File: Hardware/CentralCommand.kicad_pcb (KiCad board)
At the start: 4 copper layers, 54 parts, among them IC101 STM32F030C8, IC201 FT232RQ, P101 I2C, P102 GPIO1, P103 GPIO1, P104 USART, P105 SPI, P106 ADC, P201 USB_OTG, P202 POWER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

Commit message: converted VCCIO to 3V3 and added 1x2 power and gnd
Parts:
- added P203: 3V3, Pin_Headers:Pin_Header_Straight_1x02, F.Cu at (126.2, 56.9)
- C107: footprint Capacitors_SMD:C_1206 -> Capacitors_SMD:C_0805
- R205, R206: value 330 -> 270
- R306, R307: value 10K -> 4.7K
- TP201: value TEST -> V-IN
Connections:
- IC201 pad 1: Net-(C202-Pad1) -> Net-(C204-Pad1)
- R205 pad 2: Net-(C202-Pad1) -> Net-(C204-Pad1)
- R206 pad 2: Net-(C202-Pad1) -> Net-(C204-Pad1)
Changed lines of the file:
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@@
 (kicad_pcb (version 4) (host pcbnew 4.0.5)
   (general
-    (links 154)
-    (no_connects 121)
-    (area 97.8916 61.1886 155.727401 131.597401)
+    (links 156)
+    (no_connects 124)
+    (area 0 0 0 0)
     (thickness 1.6)
     (drawings 0)
     (tracks 76)
     (zones 0)
-    (modules 54)
+    (modules 55)
     (nets 66)
   )
@@
     )
   )
-  (module Capacitors_SMD:C_1206 (layer F.Cu)
-    (at 123.2027 100.6094 180)
-    (descr "Capacitor SMD 1206, reflow soldering, AVX (see smccp.pdf)")
-    (tags "capacitor 1206")
-    (attr smd)
-    (fp_text reference C107 (at 0 -2.3 180) (layer F.SilkS)
-      (effects (font (size 1 1) (thickness 0.15)))
-    )
-    (fp_text value 10nF (at 0 2.3 180) (layer F.Fab)
-      (effects (font (size 1 1) (thickness 0.15)))
-    )
-    (fp_line (start -1.6 0.8) (end -1.6 -0.8) (layer F.Fab) (width 0.15))
-    (fp_line (start 1.6 0.8) (end -1.6 0.8) (layer F.Fab) (width 0.15))
-    (fp_line (start 1.6 -0.8) (end 1.6 0.8) (layer F.Fab) (width 0.15))
-    (fp_line (start -1.6 -0.8) (end 1.6 -0.8) (layer F.Fab) (width 0.15))
-    (fp_line (start -2.3 -1.15) (end 2.3 -1.15) (layer F.CrtYd) (width 0.05))
-    (fp_line (start -2.3 1.15) (end 2.3 1.15) (layer F.CrtYd) (width 0.05))
-    (fp_line (start -2.3 -1.15) (end -2.3 1.15) (layer F.CrtYd) (width 0.05))
-    (fp_line (start 2.3 -1.15) (end 2.3 1.15) (layer F.CrtYd) (width 0.05))
-    (fp_line (start 1 -1.025) (end -1 -1.025) (layer F.SilkS) (width 0.15))
-    (fp_line (start -1 1.025) (end 1 1.025) (layer F.SilkS) (width 0.15))
-    (pad 1 smd rect (at -1.5 0 180) (size 1 1.6) (layers F.Cu F.Paste F.Mask)
-      (net 5 "Net-(C107-Pad1)"))
-    (pad 2 smd rect (at 1.5 0 180) (size 1 1.6) (layers F.Cu F.Paste F.Mask)
-      (net 2 GND))
-    (model Capacitors_SMD.3dshapes/C_1206.wrl
-      (at (xyz 0 0 0))
-      (scale (xyz 1 1 1))
-      (rotate (xyz 0 0 0))
-    )
-  )
   (module Capacitors_SMD:C_0805 (layer F.Cu)
     (at 126.9873 101.7905 90)
@@
     (fp_line (start 2.625 -2.625) (end 2.1 -2.625) (layer F.SilkS) (width 0.15))
     (pad 1 smd rect (at -2.4 -1.75 180) (size 0.7 0.25) (layers F.Cu F.Paste F.Mask)
-      (net 7 "Net-(C202-Pad1)"))
+      (net 8 "Net-(C204-Pad1)"))
     (pad 2 smd rect (at -2.4 -1.25 180) (size 0.7 0.25) (layers F.Cu F.Paste F.Mask)
       (net 35 "Net-(IC201-Pad2)"))
@@
       (effects (font (size 1 1) (thickness 0.15)) (justify mirror))
     )
-    (fp_text value 330 (at 0 -2.1 270) (layer B.Fab)
+    (fp_text value 270 (at 0 -2.1 270) (layer B.Fab)
       (effects (font (size 1 1) (thickness 0.15)) (justify mirror))
     )
@@
       (net 12 "Net-(D203-Pad2)"))
     (pad 2 smd rect (at 0.95 0 270) (size 0.7 1.3) (layers B.Cu B.Paste B.Mask)
-      (net 7 "Net-(C202-Pad1)"))
+      (net 8 "Net-(C204-Pad1)"))
     (model Resistors_SMD.3dshapes/R_0805.wrl
       (at (xyz 0 0 0))
@@
       (effects (font (size 1 1) (thickness 0.15)) (justify mirror))
     )
-    (fp_text value 330 (at 0 -2.1 270) (layer B.Fab)
+    (fp_text value 270 (at 0 -2.1 270) (layer B.Fab)
       (effects (font (size 1 1) (thickness 0.15)) (justify mirror))
     )
@@
       (net 14 "Net-(D204-Pad2)"))
     (pad 2 smd rect (at 0.95 0 270) (size 0.7 1.3) (layers B.Cu B.Paste B.Mask)
-      (net 7 "Net-(C202-Pad1)"))
+      (net 8 "Net-(C204-Pad1)"))
     (model Resistors_SMD.3dshapes/R_0805.wrl
       (at (xyz 0 0 0))
@@
       (effects (font (size 1 1) (thickness 0.15)))
     )
-    (fp_text value 10K (at 0 2.1) (layer F.Fab)
+    (fp_text value 4.7K (at 0 2.1) (layer F.Fab)
       (effects (font (size 1 1) (thickness 0.15)))
     )
@@
       (effects (font (size 1 1) (thickness 0.15)))
     )
-    (fp_text value 10K (at 0 2.1) (layer F.Fab)
+    (fp_text value 4.7K (at 0 2.1) (layer F.Fab)
       (effects (font (size 1 1) (thickness 0.15)))
     )
@@
       (effects (font (size 1 1) (thickness 0.15)))
     )
-    (fp_text value TEST (at 0 2) (layer F.Fab)
+    (fp_text value V-IN (at 0 2) (layer F.Fab)
       (effects (font (size 1 1) (thickness 0.15)))
     )
@@
       (net 3 "Net-(C102-Pad1)"))
   )
-  (segment (start 128.7018 67.9417) (end 126.9078 67.9417) (width 0.127) (layer B.Cu) (net 2) (status 400000))
+  (module Capacitors_SMD:C_0805 (layer F.Cu)
+    (at 123.2027 100.6094 180)
+    (descr "Capacitor SMD 0805, reflow soldering, AVX (see smccp.pdf)")
+    (tags "capacitor 0805")
+    (attr smd)
+    (fp_text reference C107 (at 0 -2.1 180) (layer F.SilkS)
+      (effects (font (size 1 1) (thickness 0.15)))
+    )
+    (fp_text value 10nF (at 0 2.1 180) (layer F.Fab)
+      (effects (font (size 1 1) (thickness 0.15)))
+    )
+    (fp_line (start -1 0.625) (end -1 -0.625) (layer F.Fab) (width 0.15))
+    (fp_line (start 1 0.625) (end -1 0.625) (layer F.Fab) (width 0.15))
+    (fp_line (start 1 -0.625) (end 1 0.625) (layer F.Fab) (width 0.15))
+    (fp_line (start -1 -0.625) (end 1 -0.625) (layer F.Fab) (width 0.15))
+    (fp_line (start -1.8 -1) (end 1.8 -1) (layer F.CrtYd) (width 0.05))
+    (fp_line (start -1.8 1) (end 1.8 1) (layer F.CrtYd) (width 0.05))
+    (fp_line (start -1.8 -1) (end -1.8 1) (layer F.CrtYd) (width 0.05))
+    (fp_line (start 1.8 -1) (end 1.8 1) (layer F.CrtYd) (width 0.05))
+    (fp_line (start 0.5 -0.85) (end -0.5 -0.85) (layer F.SilkS) (width 0.15))
+    (fp_line (start -0.5 0.85) (end 0.5 0.85) (layer F.SilkS) (width 0.15))
+    (pad 1 smd rect (at -1 0 180) (size 1 1.25) (layers F.Cu F.Paste F.Mask)
+      (net 5 "Net-(C107-Pad1)"))
+    (pad 2 smd rect (at 1 0 180) (size 1 1.25) (layers F.Cu F.Paste F.Mask)
+      (net 2 GND))
+    (model Capacitors_SMD.3dshapes/C_0805.wrl
+      (at (xyz 0 0 0))
+      (scale (xyz 1 1 1))
+      (rotate (xyz 0 0 0))
+    )
+  )
+  (module Pin_Headers:Pin_Header_Straight_1x02 (layer F.Cu)
+    (at 126.238 56.896)
+    (descr "Through hole pin header")
+    (tags "pin header")
+    (fp_text reference P203 (at 0 -5.1) (layer F.SilkS)
+      (effects (font (size 1 1) (thickness 0.15)))
+    )
+    (fp_text value 3V3 (at 0 -3.1) (layer F.Fab)
+      (effects (font (size 1 1) (thickness 0.15)))
+    )
+    (fp_line (start 1.27 1.27) (end 1.27 3.81) (layer F.SilkS) (width 0.15))
+    (fp_line (start 1.55 -1.55) (end 1.55 0) (layer F.SilkS) (width 0.15))
+    (fp_line (start -1.75 -1.75) (end -1.75 4.3) (layer F.CrtYd) (width 0.05))
+    (fp_line (start 1.75 -1.75) (end 1.75 4.3) (layer F.CrtYd) (width 0.05))
+    (fp_line (start -1.75 -1.75) (end 1.75 -1.75) (layer F.CrtYd) (width 0.05))
+    (fp_line (start -1.75 4.3) (end 1.75 4.3) (layer F.CrtYd) (width 0.05))
+    (fp_line (start 1.27 1.27) (end -1.27 1.27) (layer F.SilkS) (width 0.15))
+    (fp_line (start -1.55 0) (end -1.55 -1.55) (layer F.SilkS) (width 0.15))
+    (fp_line (start -1.55 -1.55) (end 1.55 -1.55) (layer F.SilkS) (width 0.15))
+    (fp_line (start -1.27 1.27) (end -1.27 3.81) (layer F.SilkS) (width 0.15))
+    (fp_line (start -1.27 3.81) (end 1.27 3.81) (layer F.SilkS) (width 0.15))
+    (pad 1 thru_hole rect (at 0 0) (size 2.032 2.032) (drill 1.016) (layers *.Cu *.Mask)
+      (net 4 /PWR))
+    (pad 2 thru_hole oval (at 0 2.54) (size 2.032 2.032) (drill 1.016) (layers *.Cu *.Mask)
+      (net 2 GND))
+    (model Pin_Headers.3dshapes/Pin_Header_Straight_1x02.wrl
+      (at (xyz 0 -0.05 0))
+      (scale (xyz 1 1 1))
+      (rotate (xyz 0 0 90))
+    )
+  )
+  (segment (start 128.7018 67.9417) (end 126.9078 67.9417) (width 0.127) (layer B.Cu) (net 2))
   (via (at 126.8857 67.9196) (size 0.4572) (drill 0.254) (layers F.Cu B.Cu) (net 2))
   (segment (start 126.9078 67.9417) (end 126.8857 67.9196) (width 0.127) (layer B.Cu) (net 2))
-  (segment (start 132.817 67.7915) (end 131.9033 67.7915) (width 0.127) (layer F.Cu) (net 2) (status 400000))
+  (segment (start 132.817 67.7915) (end 131.9033 67.7915) (width 0.127) (layer F.Cu) (net 2))
   (via (at 131.2672 68.4276) (size 0.4572) (drill 0.254) (layers F.Cu B.Cu) (net 2))
   (segment (start 131.9033 67.7915) (end 131.2672 68.4276) (width 0.127) (layer F.Cu) (net 2))
-  (segment (start 139.217 67.7915) (end 140.499 67.7915) (width 0.127) (layer F.Cu) (net 2) (status 400000))
+  (segment (start 139.217 67.7915) (end 140.499 67.7915) (width 0.127) (layer F.Cu) (net 2))
   (via (at 140.5509 67.8434) (size 0.4572) (drill 0.254) (layers F.Cu B.Cu) (net 2))
   (segment (start 140.499 67.7915) (end 140.5509 67.8434) (width 0.127) (layer F.Cu) (net 2))
-  (segment (start 132.4966 70.8914) (end 132.6769 70.8914) (width 0.127) (layer F.Cu) (net 2) (status C00000))
-  (segment (start 132.6769 70.8914) (end 133.4516 70.1167) (width 0.127) (layer F.Cu) (net 2) (status 400000))
+  (segment (start 132.4966 70.8914) (end 132.6769 70.8914) (width 0.127) (layer F.Cu) (net 2))
+  (segment (start 132.6769 70.8914) (end 133.4516 70.1167) (width 0.127) (layer F.Cu) (net 2))
   (via (at 133.4516 70.1167) (size 0.4572) (drill 0.254) (layers F.Cu B.Cu) (net 2))
   (segment (start 137.217 65.3415) (end 137.217 65.7915) (width 0.127) (layer F.Cu) (net 2))
@@
   (segment (start 137.317 66.8447) (end 136.9822 66.5099) (width 0.127) (layer F.Cu) (net 6))
   (segment (start 128.0828 65.9417) (end 128.7018 65.9417) (width 0.127) (layer B.Cu) (net 6))
-  (segment (start 128.7396 75.1052) (end 129.1616 75.1052) (width 0.127) (layer F.Cu) (net 7))
   (segment (start 132.9477 72.2249) (end 134.7384 70.4342) (width 0.127) (layer F.Cu) (net 7))
   (segment (start 132.0419 72.2249) (end 132.9477 72.2249) (width 0.127) (layer F.Cu) (net 7))
   (segment (start 129.1616 75.1052) (end 132.0419 72.2249) (width 0.127) (layer F.Cu) (net 7))
+  (segment (start 128.7396 75.1052) (end 129.1616 75.1052) (width 0.127) (layer F.Cu) (net 8))
   (segment (start 137.9474 71.8693) (end 137.9474 72.898) (width 0.127) (layer F.Cu) (net 9))
   (segment (start 138.3665 73.3171) (end 139.2588 73.3171) (width 0.127) (layer F.Cu) (net 9))

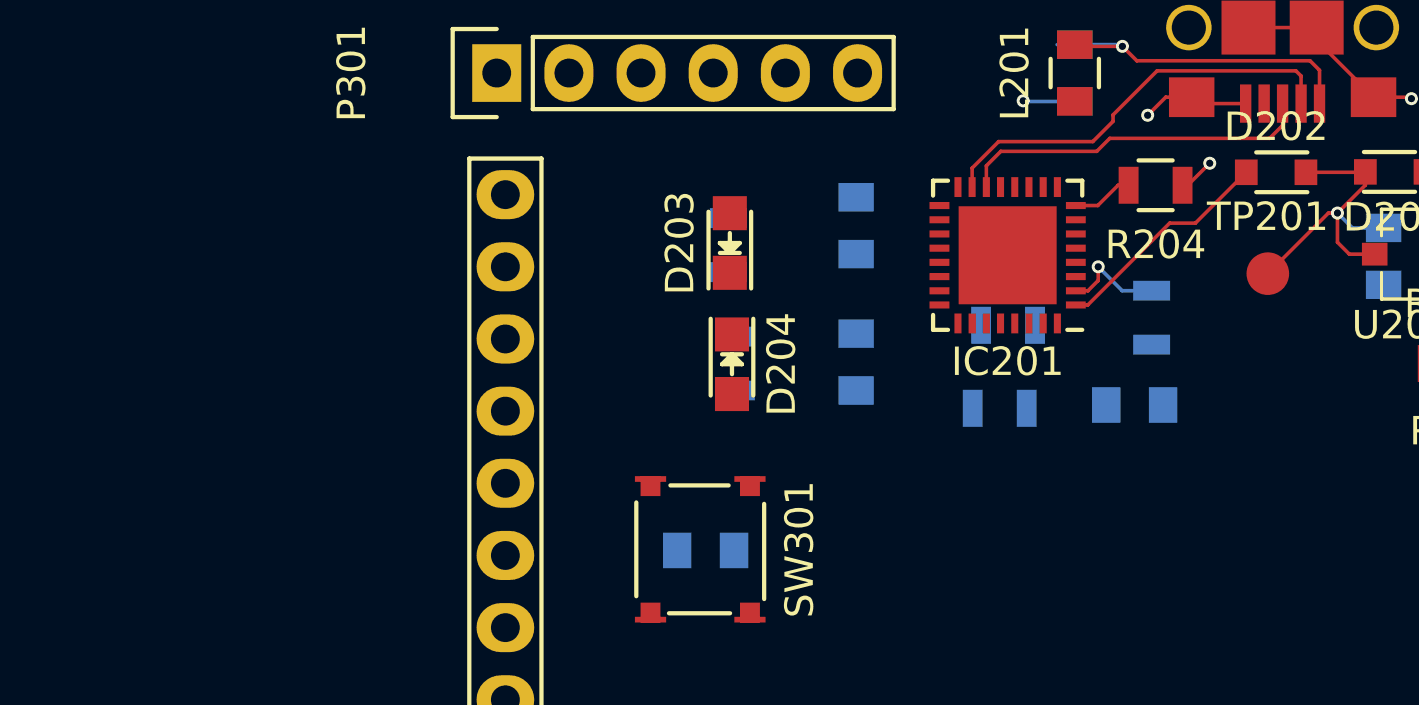
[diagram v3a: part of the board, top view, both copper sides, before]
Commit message: swapped power and gnd on gpio headers and added blinky led
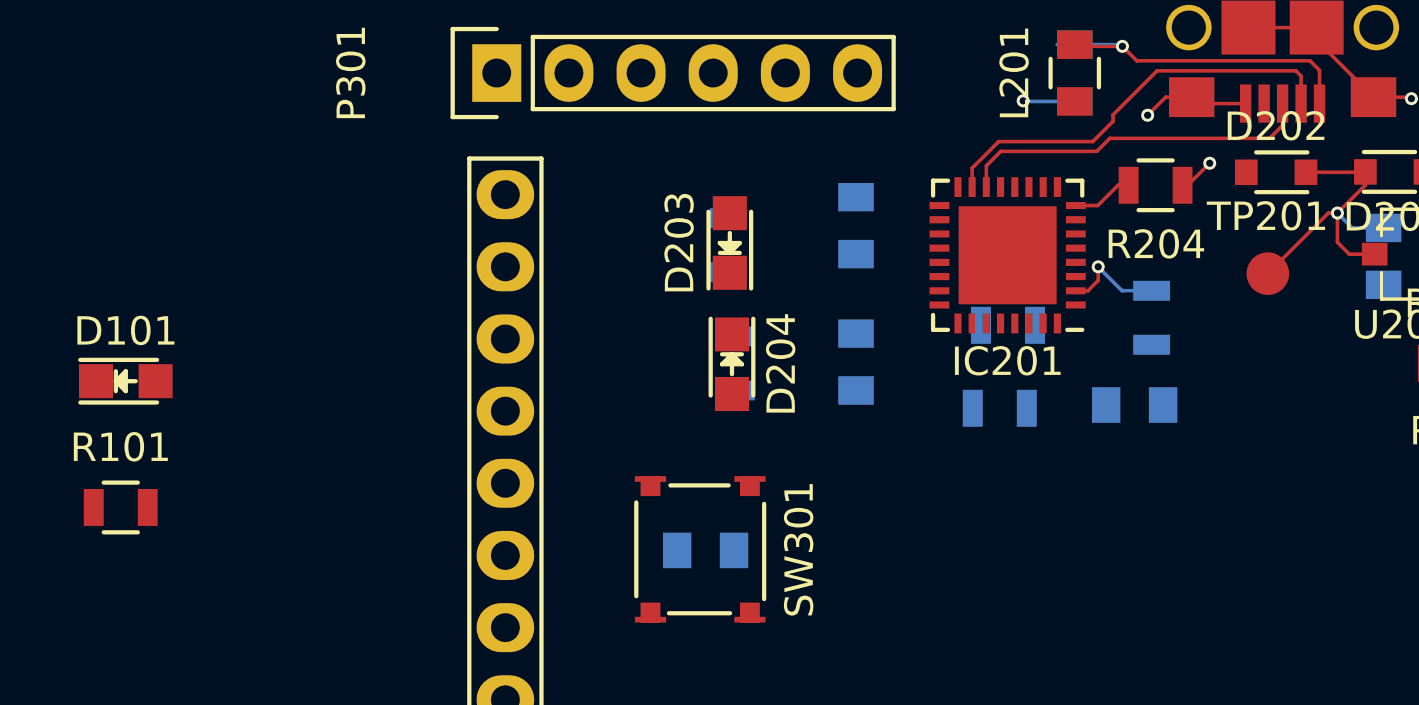
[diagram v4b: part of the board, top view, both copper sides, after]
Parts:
- added D101: RED LED, LEDs:LED_0805, F.Cu at (95.3, 77.8)
- added R101: 270, Resistors_SMD:R_0805, F.Cu at (95.1, 82.2)
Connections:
- P102 pad 1: GND -> /PWR
- P102 pad 2: /PWR -> GND
- P103 pad 1: GND -> /PWR
- P103 pad 2: /PWR -> GND
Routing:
- net Net-(C202-Pad1): track 7.51 -> 0.00 mm
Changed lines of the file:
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@@
 (kicad_pcb (version 4) (host pcbnew 4.0.5)
   (general
-    (links 156)
-    (no_connects 124)
+    (links 159)
+    (no_connects 129)
     (area 0 0 0 0)
     (thickness 1.6)
     (drawings 0)
-    (tracks 76)
+    (tracks 72)
     (zones 0)
-    (modules 55)
-    (nets 66)
+    (modules 57)
+    (nets 67)
   )
   (page A4)
@@
   (net 64 "Net-(IC201-Pad14)")
   (net 65 "Net-(IC201-Pad15)")
+  (net 66 "Net-(D101-Pad2)")
   (net_class Default "This is the default net class."
     (clearance 0.127)
@@
     (add_net "Net-(C204-Pad1)")
     (add_net "Net-(C205-Pad1)")
+    (add_net "Net-(D101-Pad2)")
     (add_net "Net-(D201-Pad2)")
     (add_net "Net-(D203-Pad2)")
@@
     (fp_line (start -1.55 -1.55) (end 1.55 -1.55) (layer F.SilkS) (width 0.15))
     (pad 1 thru_hole rect (at 0 0 180) (size 2.032 1.7272) (drill 1.016) (layers *.Cu *.Mask)
-      (net 2 GND))
+      (net 4 /PWR))
     (pad 2 thru_hole oval (at 0 2.54 180) (size 2.032 1.7272) (drill 1.016) (layers *.Cu *.Mask)
-      (net 4 /PWR))
+      (net 2 GND))
     (pad 3 thru_hole oval (at 0 5.08 180) (size 2.032 1.7272) (drill 1.016) (layers *.Cu *.Mask)
       (net 44 /PC13))
@@
     (fp_line (start -1.55 -1.55) (end 1.55 -1.55) (layer F.SilkS) (width 0.15))
     (pad 1 thru_hole rect (at 0 0 180) (size 2.032 1.7272) (drill 1.016) (layers *.Cu *.Mask)
-      (net 2 GND))
+      (net 4 /PWR))
     (pad 2 thru_hole oval (at 0 2.54 180) (size 2.032 1.7272) (drill 1.016) (layers *.Cu *.Mask)
-      (net 4 /PWR))
+      (net 2 GND))
     (pad 3 thru_hole oval (at 0 5.08 180) (size 2.032 1.7272) (drill 1.016) (layers *.Cu *.Mask)
       (net 60 /PA12))
@@
     )
   )
+  (module LEDs:LED_0805 (layer F.Cu)
+    (at 95.3008 77.7875)
+    (descr "LED 0805 smd package")
+    (tags "LED 0805 SMD")
+    (attr smd)
+    (fp_text reference D101 (at 0 -1.75) (layer F.SilkS)
+      (effects (font (size 1 1) (thickness 0.15)))
+    )
+    (fp_text value "RED LED" (at 0 1.75) (layer F.Fab)
+      (effects (font (size 1 1) (thickness 0.15)))
+    )
+    (fp_line (start -0.4 -0.3) (end -0.4 0.3) (layer F.Fab) (width 0.15))
+    (fp_line (start -0.3 0) (end 0 -0.3) (layer F.Fab) (width 0.15))
+    (fp_line (start 0 0.3) (end -0.3 0) (layer F.Fab) (width 0.15))
+    (fp_line (start 0 -0.3) (end 0 0.3) (layer F.Fab) (width 0.15))
+    (fp_line (start 1 -0.6) (end -1 -0.6) (layer F.Fab) (width 0.15))
+    (fp_line (start 1 0.6) (end 1 -0.6) (layer F.Fab) (width 0.15))
+    (fp_line (start -1 0.6) (end 1 0.6) (layer F.Fab) (width 0.15))
+    (fp_line (start -1 -0.6) (end -1 0.6) (layer F.Fab) (width 0.15))
+    (fp_line (start -1.6 0.75) (end 1.1 0.75) (layer F.SilkS) (width 0.15))
+    (fp_line (start -1.6 -0.75) (end 1.1 -0.75) (layer F.SilkS) (width 0.15))
+    (fp_line (start -0.1 0.15) (end -0.1 -0.1) (layer F.SilkS) (width 0.15))
+    (fp_line (start -0.1 -0.1) (end -0.25 0.05) (layer F.SilkS) (width 0.15))
+    (fp_line (start -0.35 -0.35) (end -0.35 0.35) (layer F.SilkS) (width 0.15))
+    (fp_line (start 0 0) (end 0.35 0) (layer F.SilkS) (width 0.15))
+    (fp_line (start -0.35 0) (end 0 -0.35) (layer F.SilkS) (width 0.15))
+    (fp_line (start 0 -0.35) (end 0 0.35) (layer F.SilkS) (width 0.15))
+    (fp_line (start 0 0.35) (end -0.35 0) (layer F.SilkS) (width 0.15))
+    (fp_line (start 1.9 -0.95) (end 1.9 0.95) (layer F.CrtYd) (width 0.05))
+    (fp_line (start 1.9 0.95) (end -1.9 0.95) (layer F.CrtYd) (width 0.05))
+    (fp_line (start -1.9 0.95) (end -1.9 -0.95) (layer F.CrtYd) (width 0.05))
+    (fp_line (start -1.9 -0.95) (end 1.9 -0.95) (layer F.CrtYd) (width 0.05))
+    (pad 2 smd rect (at 1.04902 0 180) (size 1.19888 1.19888) (layers F.Cu F.Paste F.Mask)
+      (net 66 "Net-(D101-Pad2)"))
+    (pad 1 smd rect (at -1.04902 0 180) (size 1.19888 1.19888) (layers F.Cu F.Paste F.Mask)
+      (net 2 GND))
+    (model LEDs.3dshapes/LED_0805.wrl
+      (at (xyz 0 0 0))
+      (scale (xyz 1 1 1))
+      (rotate (xyz 0 0 0))
+    )
+  )
+  (module Resistors_SMD:R_0805 (layer F.Cu)
+    (at 95.123 82.2325)
+    (descr "Resistor SMD 0805, reflow soldering, Vishay (see dcrcw.pdf)")
+    (tags "resistor 0805")
+    (attr smd)
+    (fp_text reference R101 (at 0 -2.1) (layer F.SilkS)
+      (effects (font (size 1 1) (thickness 0.15)))
+    )
+    (fp_text value 270 (at 0 2.1) (layer F.Fab)
+      (effects (font (size 1 1) (thickness 0.15)))
+    )
+    (fp_line (start -1 0.625) (end -1 -0.625) (layer F.Fab) (width 0.1))
+    (fp_line (start 1 0.625) (end -1 0.625) (layer F.Fab) (width 0.1))
+    (fp_line (start 1 -0.625) (end 1 0.625) (layer F.Fab) (width 0.1))
+    (fp_line (start -1 -0.625) (end 1 -0.625) (layer F.Fab) (width 0.1))
+    (fp_line (start -1.6 -1) (end 1.6 -1) (layer F.CrtYd) (width 0.05))
+    (fp_line (start -1.6 1) (end 1.6 1) (layer F.CrtYd) (width 0.05))
+    (fp_line (start -1.6 -1) (end -1.6 1) (layer F.CrtYd) (width 0.05))
+    (fp_line (start 1.6 -1) (end 1.6 1) (layer F.CrtYd) (width 0.05))
+    (fp_line (start 0.6 0.875) (end -0.6 0.875) (layer F.SilkS) (width 0.15))
+    (fp_line (start -0.6 -0.875) (end 0.6 -0.875) (layer F.SilkS) (width 0.15))
+    (pad 1 smd rect (at -0.95 0) (size 0.7 1.3) (layers F.Cu F.Paste F.Mask)
+      (net 58 /PB15))
+    (pad 2 smd rect (at 0.95 0) (size 0.7 1.3) (layers F.Cu F.Paste F.Mask)
+      (net 66 "Net-(D101-Pad2)"))
+    (model Resistors_SMD.3dshapes/R_0805.wrl
+      (at (xyz 0 0 0))
+      (scale (xyz 1 1 1))
+      (rotate (xyz 0 0 0))
+    )
+  )
   (segment (start 128.7018 67.9417) (end 126.9078 67.9417) (width 0.127) (layer B.Cu) (net 2))
   (via (at 126.8857 67.9196) (size 0.4572) (drill 0.254) (layers F.Cu B.Cu) (net 2))
@@
   (segment (start 137.317 66.8447) (end 136.9822 66.5099) (width 0.127) (layer F.Cu) (net 6))
   (segment (start 128.0828 65.9417) (end 128.7018 65.9417) (width 0.127) (layer B.Cu) (net 6))
-  (segment (start 132.9477 72.2249) (end 134.7384 70.4342) (width 0.127) (layer F.Cu) (net 7))
-  (segment (start 132.0419 72.2249) (end 132.9477 72.2249) (width 0.127) (layer F.Cu) (net 7))
-  (segment (start 129.1616 75.1052) (end 132.0419 72.2249) (width 0.127) (layer F.Cu) (net 7))
-  (segment (start 128.7396 75.1052) (end 129.1616 75.1052) (width 0.127) (layer F.Cu) (net 8))
   (segment (start 137.9474 71.8693) (end 137.9474 72.898) (width 0.127) (layer F.Cu) (net 9))
   (segment (start 138.3665 73.3171) (end 139.2588 73.3171) (width 0.127) (layer F.Cu) (net 9))

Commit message: more layout
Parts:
- removed P203: 3V3, Pin_Headers:Pin_Header_Straight_1x02
- C202, C203, C204, C205, C206, R201, R202, R203, R207: moved to F.Cu
- moved C101 43.6 mm to (87.0, 105.2), turned to 270 degrees
- moved C104 36.4 mm to (87.1, 99.7), turned to 90 degrees
- moved C102 35.7 mm to (90.0, 105.3), turned to 270 degrees
- moved C107 33.4 mm to (89.8, 99.7), turned to 270 degrees
- moved C108 31.2 mm to (95.9, 105.1)
- moved C103 27.9 mm to (92.9, 99.7)
- moved C105 27.2 mm to (96.8, 99.6), turned to 90 degrees
- moved R207 24.9 mm to (153.3, 48.3), turned to 90 degrees
- moved L101 24.3 mm to (99.1, 105.6), turned to 270 degrees
- moved C106 23.9 mm to (92.5, 105.6)
- moved SW301 23.8 mm to (93.8, 93.5)
- moved C301 21.7 mm to (94.4, 88.0)
- moved D205 20.7 mm to (153.5, 52.9), turned to 90 degrees
- moved R307 18.9 mm to (160.9, 76.0)
- moved R306 18.4 mm to (160.5, 79.2)
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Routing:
- net Net-(C202-Pad1): track 0.00 -> 25.9 mm
- net GND: track 13.9 -> 34.0 mm, vias 4 -> 11
- net Net-(C204-Pad1): track 0.00 -> 19.6 mm, vias 0 -> 2
- net Net-(IC201-Pad15): track 14.8 -> 0.00 mm
- net Net-(IC201-Pad14): track 12.5 -> 0.00 mm
- net Net-(C205-Pad1): track 11.6 -> 18.6 mm, vias 1 -> 0
- net Net-(C201-Pad1): track 12.5 -> 5.96 mm
- net /power/RXLED: track 0.00 -> 5.01 mm
- net Net-(IC201-Pad30): track 0.00 -> 3.38 mm
- net Net-(IC201-Pad32): track 0.00 -> 2.71 mm
- net /power/TXLED: track 0.00 -> 2.14 mm
- net Net-(D203-Pad2): track 0.00 -> 1.99 mm, vias 0 -> 1
- net Net-(D204-Pad2): track 0.00 -> 1.99 mm, vias 0 -> 1
- net Net-(IC201-Pad2): track 3.65 -> 4.45 mm, vias 1 -> 0
